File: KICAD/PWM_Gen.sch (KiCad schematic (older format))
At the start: 0 parts

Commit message: labels dans les blocks
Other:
- note added: "Astuce: utilisez le ~~ devant un label pour créer des signaux ~barre"
- note added: "Entrées"
- note added: "Sorties"
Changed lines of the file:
@@
 Comment4 ""
 $EndDescr
+Text HLabel 5150 3050 0    50   Input ~ 0
+Ramp
+Text HLabel 5150 3150 0    50   Input ~ 0
+Feedback
+Text HLabel 5450 3050 2    50   Output ~ 0
+PWM
+Text HLabel 5450 3150 2    50   Output ~ 0
+~PWM
+Text Notes 4850 3300 0    50   ~ 0
+Entrées
+Text Notes 4050 3600 0    50   ~ 0
+Astuce: utilisez le ~~ devant un label pour créer des signaux ~barre
+Text Notes 5450 3300 0    50   ~ 0
+Sorties
+Wire Notes Line
+	5400 2950 5800 2950
+Wire Notes Line
+	5800 2950 5800 3350
+Wire Notes Line
+	5800 3350 5400 3350
+Wire Notes Line
+	5400 2950 5400 3350
+Wire Notes Line
+	5250 2950 5250 3350
+Wire Notes Line
+	5250 3350 4700 3350
+Wire Notes Line
+	4700 3350 4700 2950
+Wire Notes Line
+	4700 2950 5250 2950
 $EndSCHEMATC

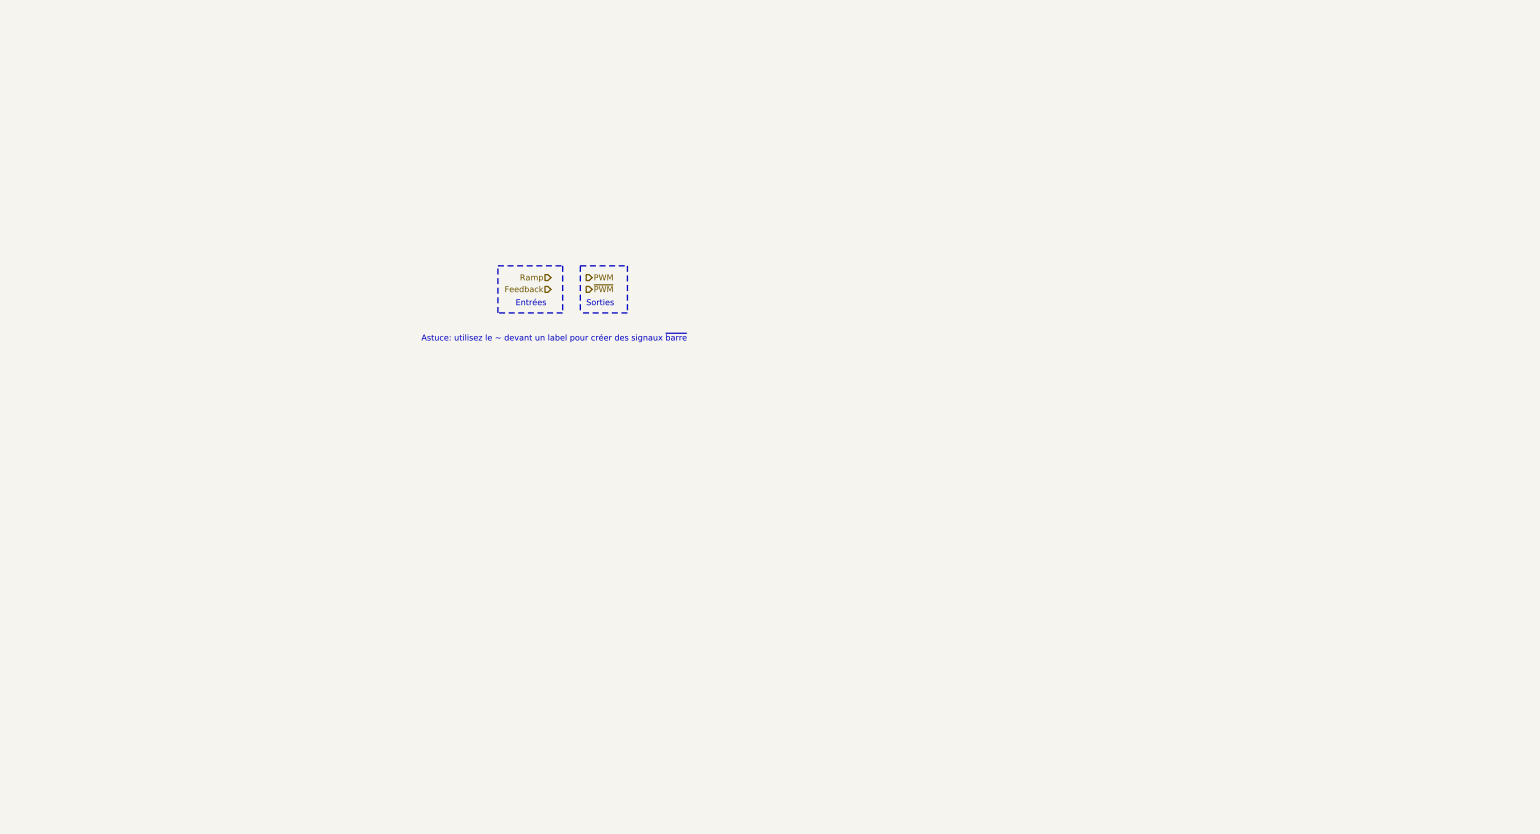
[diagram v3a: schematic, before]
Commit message: added draft pwm gen & pid
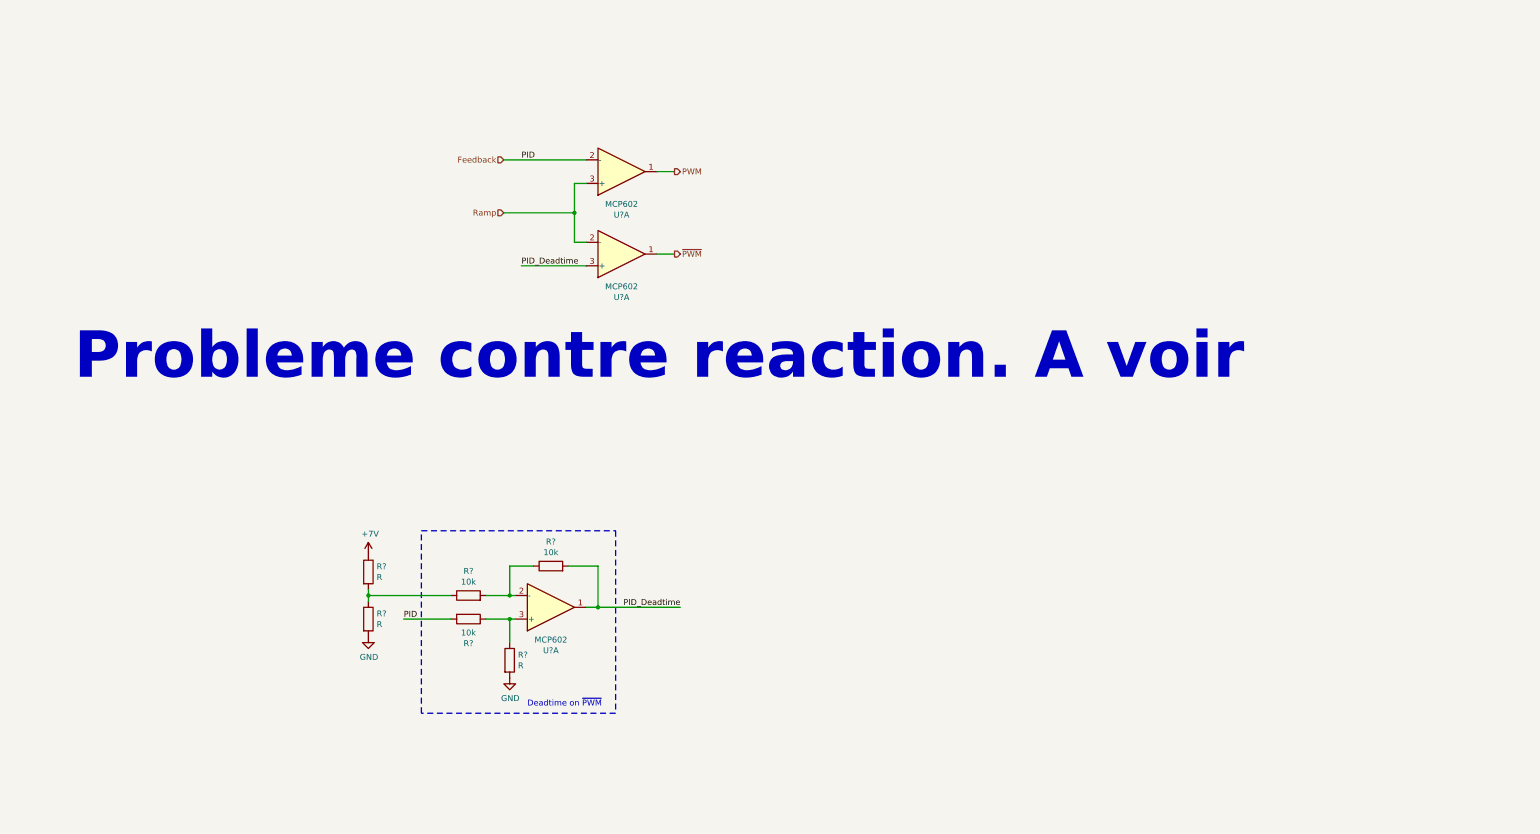
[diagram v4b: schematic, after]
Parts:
- added R? (x3): 10k, symbol Device:R
- added R? (x3): R, symbol Device:R
- added U? (x3): MCP602, symbol Amplifier_Operational:MCP602
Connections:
- net Feedback: now also R?.2, U?.2 (-)
- net PWM: now also U?.1
- net Ramp: now also U?.2 (-), U?.3 (+)
- net ~PWM: now also U?.1
- new net: R?.1, R?.2, U?.2 (-)
- new net: R?.1, R?.1, U?.3 (+)
- new net: R?.1, R?.1, R?.2
- new net +7V: R?.1
- new net GND: R?.2, R?.2
- new net PID_Deadtime: R?.2, U?.1, U?.3 (+)
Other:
- note added: "Deadtime on ~PWM"
- note added: "Probleme contre reaction. A voir\n"
- note removed: "Astuce: utilisez le ~~ devant un label pour créer des signaux ~barre"
- note removed: "Entrées"
- note removed: "Sorties"

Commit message: a ton of new stuff. V0.8
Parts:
- added C?: 100n, symbol Device:C
- added U?: MCP602, symbol Amplifier_Operational:MCP602
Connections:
- net Feedback: now also U?.3 (+); no longer U?.2 (-)
- net GND: now also C?.2, U?.8 (V+)
- net PID_Deadtime: no longer U?.3 (+)
- net Ramp: now also U?.2 (-), U?.3 (+); no longer U?.2 (-), U?.3 (+)
- net VDeadTime: now reaches R?.1, R?.1, R?.2
- net +7V renamed VREF
- new net Feedback_Deadtime: U?.2 (-)
- new net VCC: C?.1, U?.4 (V-)
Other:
- note added: "Tension deadtime"
- moved on the sheet: R?, U?A

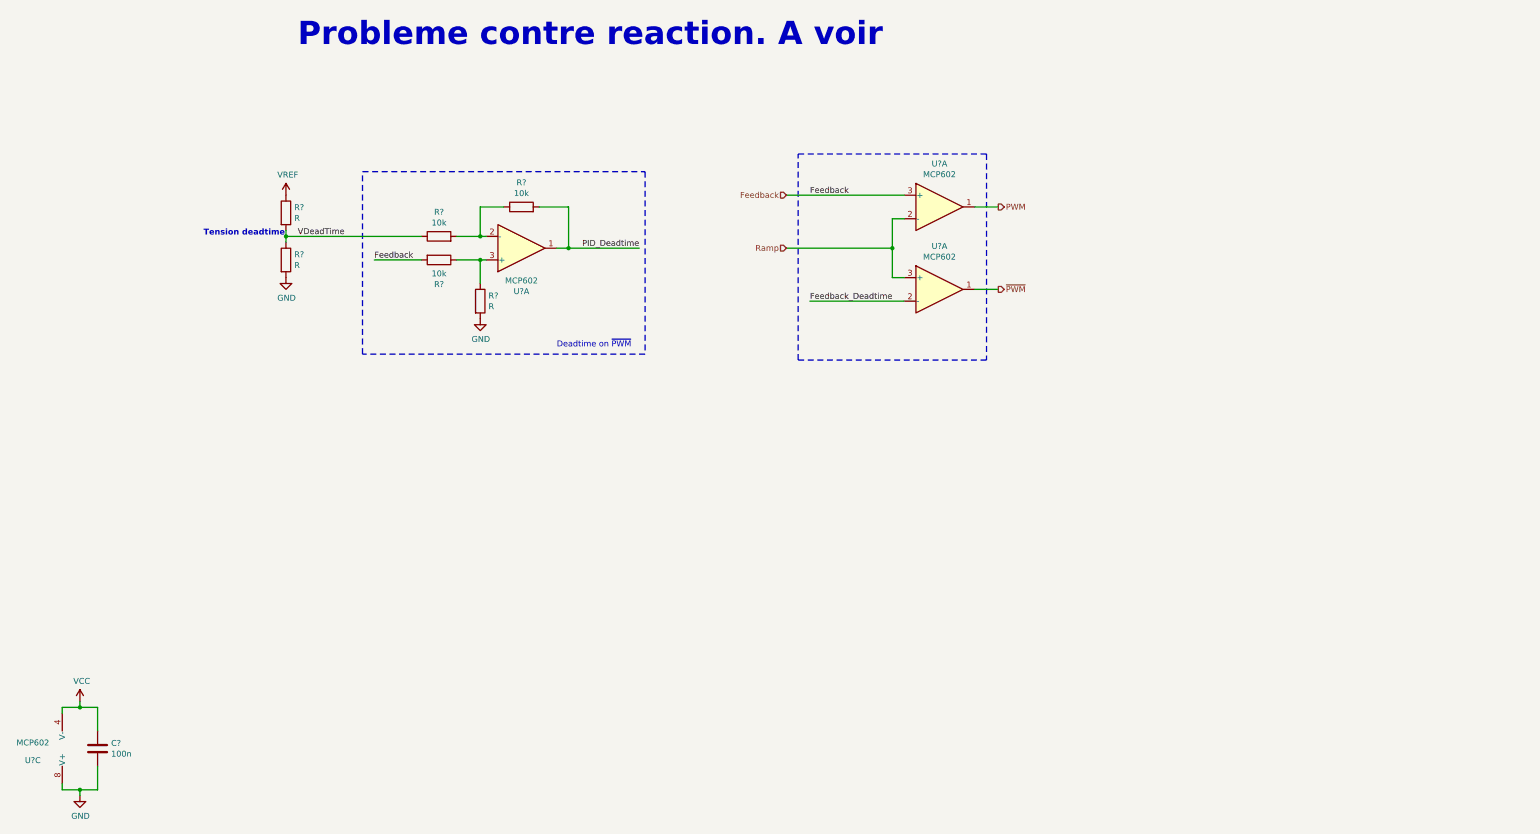
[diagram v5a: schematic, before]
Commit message: PID + PWM + RAMP finished
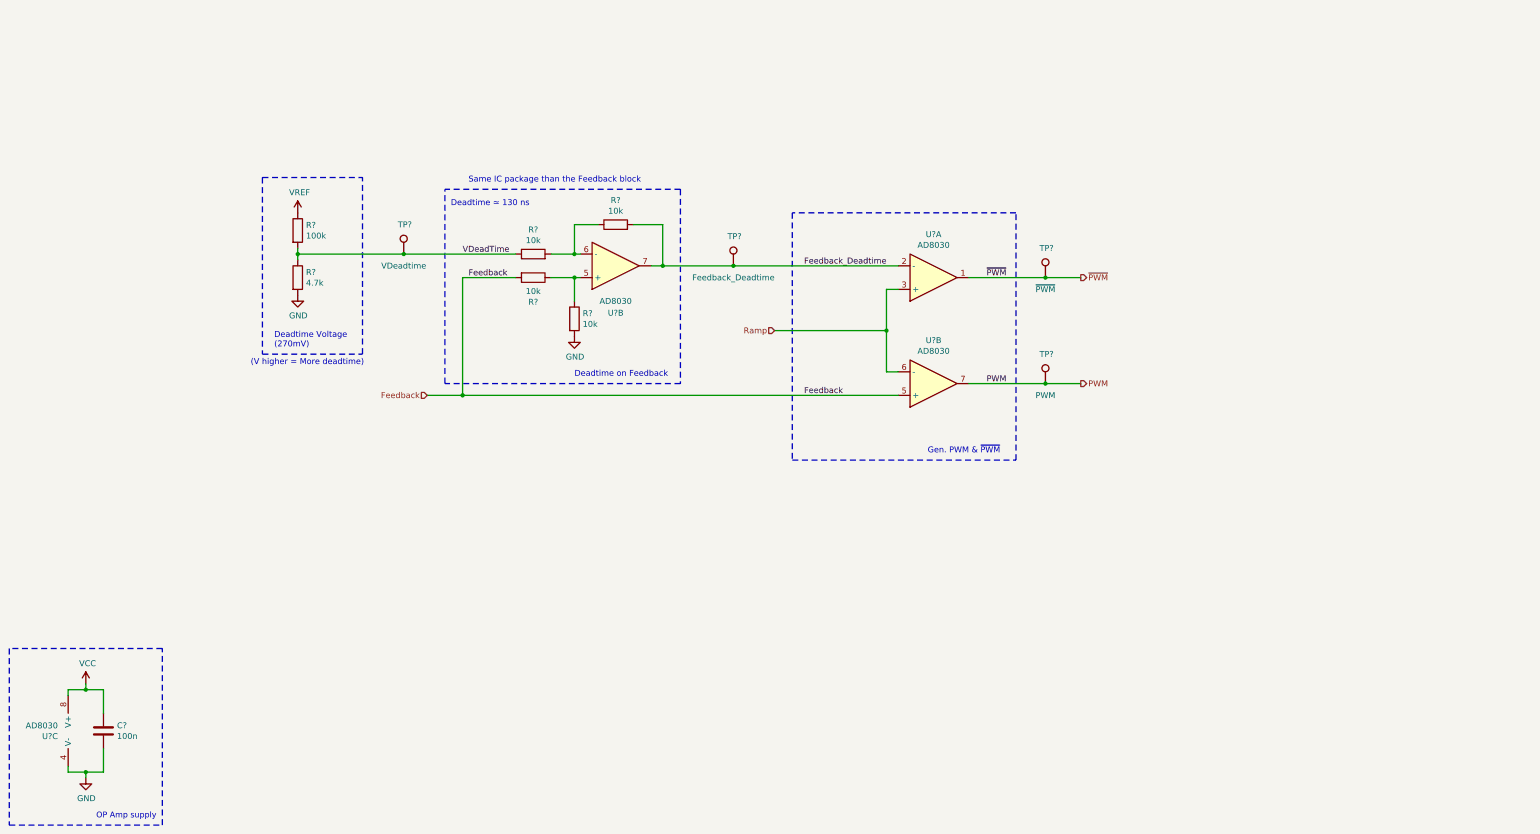
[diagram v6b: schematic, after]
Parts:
- removed C?: 100n, symbol Device:C
- removed U? (x4): MCP602, symbol Amplifier_Operational:MCP602
- added C?: 100n, Capacitor_SMD:C_0805_2012Metric_Pad1.15x1.40mm_HandSolder, symbol Device:C
- added TP?: VDeadtime, symbol Connector:TestPoint
- added TP?: Feedback_Deadtime, symbol Connector:TestPoint
- added TP?: ~PWM, symbol Connector:TestPoint
- added TP?: PWM, symbol Connector:TestPoint
- added U? (x4): AD8030, symbol Sesame:AD8030
- R? (x3): footprint (none) -> Resistor_SMD:R_0805_2012Metric_Pad1.15x1.40mm_HandSolder
- R?: value R -> 10k; footprint (none) -> Resistor_SMD:R_0805_2012Metric_Pad1.15x1.40mm_HandSolder
- R?: value R -> 100k; footprint (none) -> Resistor_SMD:R_0805_2012Metric_Pad1.15x1.40mm_HandSolder
- R?: value R -> 4.7k; footprint (none) -> Resistor_SMD:R_0805_2012Metric_Pad1.15x1.40mm_HandSolder
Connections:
- net PID_Deadtime is gone; now on net Feedback_Deadtime: R?.2
- net Feedback: now also U?.5 (+)
- net Feedback_Deadtime: now also TP?.1, U?.2 (-), U?.7
- net GND: now also C?.2, U?.4 (V-)
- net PWM: now also TP?.1, U?.7
- net Ramp: now also U?.3 (+), U?.6 (-)
- net VCC: now also C?.1, U?.8 (V+)
- net VDeadTime: now also TP?.1
- net ~PWM: now also TP?.1, U?.1
- net at R?.1, R?.2: now also U?.6 (-)
- net at R?.1, R?.1: now also U?.5 (+)
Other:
- note added: "(V higher = More deadtime)"
- note added: "Deadtime Voltage\n(270mV)"
- note added: "Deadtime on Feedback"
- note added: "Deadtime ≃ 130 ns"
- note added: "Gen. PWM & ~PWM"
- note added: "OP Amp supply"
- note added: "Same IC package than the Feedback block"
- note removed: "Deadtime on ~PWM"
- note removed: "Probleme contre reaction. A voir\n"
- note removed: "Tension deadtime"
- moved on the sheet: R?

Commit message: mainly footprints
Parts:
- U1, U2: renamed from U?; footprint (none) -> Package_SO:SO-8_3.9x4.9mm_P1.27mm
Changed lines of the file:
@@
 $Descr A4 11693 8268
 encoding utf-8
-Sheet 3 16
+Sheet 2 16
 Title "SESAME"
 Date ""
@@
 Same IC package than the Feedback block
 $Comp
-L Sesame:AD8030 U?
+L Sesame:AD8030 U2
 U 1 1 6128401D
 P 8400 3050
-F 0 "U?" H 8400 2683 50  0000 C CNN
+F 0 "U2" H 8400 2683 50  0000 C CNN
 F 1 "AD8030" H 8400 2774 50  0000 C CNN
-F 2 "" H 8400 3050 50  0001 C CNN
+F 2 "Package_SO:SO-8_3.9x4.9mm_P1.27mm" H 8400 3050 50  0001 C CNN
 F 3 "~" H 8400 3050 50  0001 C CNN
 	1    8400 3050
@@
 $EndComp
 $Comp
-L Sesame:AD8030 U?
+L Sesame:AD8030 U2
 U 2 1 61284FE7
 P 8400 3950
-F 0 "U?" H 8400 3583 50  0000 C CNN
+F 0 "U2" H 8400 3583 50  0000 C CNN
 F 1 "AD8030" H 8400 3674 50  0000 C CNN
-F 2 "" H 8400 3950 50  0001 C CNN
+F 2 "Package_SO:SO-8_3.9x4.9mm_P1.27mm" H 8400 3950 50  0001 C CNN
 F 3 "~" H 8400 3950 50  0001 C CNN
 	2    8400 3950
@@
 $EndComp
 $Comp
-L Sesame:AD8030 U?
+L Sesame:AD8030 U1
 U 2 1 6128D784
 P 5700 2950
-F 0 "U?" H 5700 3350 50  0000 C CNN
+F 0 "U1" H 5700 3350 50  0000 C CNN
 F 1 "AD8030" H 5700 3250 50  0000 C CNN
-F 2 "" H 5700 2950 50  0001 C CNN
+F 2 "Package_SO:SO-8_3.9x4.9mm_P1.27mm" H 5700 2950 50  0001 C CNN
 F 3 "~" H 5700 2950 50  0001 C CNN
 	2    5700 2950
@@
 $EndComp
 $Comp
-L Sesame:AD8030 U?
+L Sesame:AD8030 U2
 U 3 1 612CB373
 P 1150 6900
-AR Path="/60F1AF26/612CB373" Ref="U?"  Part="3"
+AR Path="/60F1AF26/612CB373" Ref="U2"  Part="3"
 AR Path="/60F1B237/612CB373" Ref="U?"  Part="3"
-F 0 "U?" H 963 6854 50  0000 R CNN
+F 0 "U2" H 963 6854 50  0000 R CNN
 F 1 "AD8030" H 963 6945 50  0000 R CNN
-F 2 "" H 1150 6900 50  0001 C CNN
+F 2 "Package_SO:SO-8_3.9x4.9mm_P1.27mm" H 1150 6900 50  0001 C CNN
 F 3 "~" H 1150 6900 50  0001 C CNN
 	3    1150 6900

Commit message: revex with jmt
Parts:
- R? (x4): value 10k -> 100k
- TP?: value VDeadtime -> TP_NOP
- TP?: value Feedback_Deadtime -> TP_POP
- TP?: value ~PWM -> TP_POP
- TP?: value PWM -> TP_POP
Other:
- moved on the sheet: TP?, U2A, U2B
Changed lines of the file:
@@
 $Descr A4 11693 8268
 encoding utf-8
-Sheet 2 16
+Sheet 16 16
 Title "SESAME"
 Date ""
@@
 AR Path="/60F1AF26/613D641B" Ref="R?"  Part="1"
 F 0 "R?" V 5207 3050 50  0000 C CNN
-F 1 "10k" V 5116 3050 50  0000 C CNN
+F 1 "100k" V 5116 3050 50  0000 C CNN
 F 2 "Resistor_SMD:R_0805_2012Metric_Pad1.15x1.40mm_HandSolder" V 4930 3050 50  0001 C CNN
 F 3 "~" H 5000 3050 50  0001 C CNN
@@
 AR Path="/60F1AF26/613D6415" Ref="R?"  Part="1"
 F 0 "R?" V 5207 2850 50  0000 C CNN
-F 1 "10k" V 5116 2850 50  0000 C CNN
+F 1 "100k" V 5116 2850 50  0000 C CNN
 F 2 "Resistor_SMD:R_0805_2012Metric_Pad1.15x1.40mm_HandSolder" V 4930 2850 50  0001 C CNN
 F 3 "~" H 5000 2850 50  0001 C CNN
@@
 AR Path="/60F1AF26/613D6429" Ref="R?"  Part="1"
 F 0 "R?" H 5420 3446 50  0000 L CNN
-F 1 "10k" H 5420 3355 50  0000 L CNN
+F 1 "100k" H 5420 3355 50  0000 L CNN
 F 2 "Resistor_SMD:R_0805_2012Metric_Pad1.15x1.40mm_HandSolder" V 5280 3400 50  0001 C CNN
 F 3 "~" H 5350 3400 50  0001 C CNN
@@
 Connection ~ 6100 2950
 Wire Wire Line
-	8000 3150 8000 3500
-Wire Wire Line
-	8000 3500 8000 3850
-Connection ~ 8000 3500
-Text Notes 8350 4550 0    50   ~ 0
+	7800 3150 7800 3500
+Wire Wire Line
+	7800 3500 7800 3850
+Connection ~ 7800 3500
+Text Notes 8150 4550 0    50   ~ 0
 Gen. PWM & ~PWM
 Wire Wire Line
-	9650 3950 9350 3950
-Wire Notes Line
-	7200 4600 9100 4600
-Wire Notes Line
-	9100 4600 9100 2500
-Wire Wire Line
-	7050 3500 8000 3500
-Text Label 7300 4050 0    50   ~ 0
+	9450 3950 9150 3950
+Wire Notes Line
+	7000 4600 8900 4600
+Wire Notes Line
+	8900 4600 8900 2500
+Wire Wire Line
+	6850 3500 7800 3500
+Text Label 7100 4050 0    50   ~ 0
 Feedback
-Text Label 7300 2950 0    50   ~ 0
+Text Label 7100 2950 0    50   ~ 0
 Feedback_Deadtime
 Wire Wire Line
-	8000 3850 8100 3850
-Wire Wire Line
-	8100 3150 8000 3150
-Wire Wire Line
-	8700 3050 9350 3050
-Text HLabel 9650 3050 2    50   Output ~ 0
+	7800 3850 7900 3850
+Wire Wire Line
+	7900 3150 7800 3150
+Wire Wire Line
+	8500 3050 9150 3050
+Text HLabel 9450 3050 2    50   Output ~ 0
 ~PWM
-Text HLabel 9650 3950 2    50   Output ~ 0
+Text HLabel 9450 3950 2    50   Output ~ 0
 PWM
-Text HLabel 7050 3500 0    50   Input ~ 0
+Text HLabel 6850 3500 0    50   Input ~ 0
 Ramp
 Wire Notes Line
-	9100 2500 7200 2500
-Wire Notes Line
-	7200 2500 7200 4600
+	8900 2500 7000 2500
+Wire Notes Line
+	7000 2500 7000 4600
 Wire Wire Line
 	4100 4050 4400 4050
 Wire Wire Line
-	4400 4050 8100 4050
+	4400 4050 7900 4050
 Text Notes 4450 2250 0    50   ~ 0
 Same IC package than the Feedback block
@@
 L Sesame:AD8030 U2
 U 1 1 6128401D
-P 8400 3050
-F 0 "U2" H 8400 2683 50  0000 C CNN
-F 1 "AD8030" H 8400 2774 50  0000 C CNN
-F 2 "Package_SO:SO-8_3.9x4.9mm_P1.27mm" H 8400 3050 50  0001 C CNN
-F 3 "~" H 8400 3050 50  0001 C CNN
-	1    8400 3050
+P 8200 3050
+F 0 "U2" H 8200 2683 50  0000 C CNN
+F 1 "AD8030" H 8200 2774 50  0000 C CNN
+F 2 "Package_SO:SO-8_3.9x4.9mm_P1.27mm" H 8200 3050 50  0001 C CNN
+F 3 "~" H 8200 3050 50  0001 C CNN
+	1    8200 3050
 	1    0    0    1
 $EndComp
@@
 L Sesame:AD8030 U2
 U 2 1 61284FE7
-P 8400 3950
-F 0 "U2" H 8400 3583 50  0000 C CNN
-F 1 "AD8030" H 8400 3674 50  0000 C CNN
-F 2 "Package_SO:SO-8_3.9x4.9mm_P1.27mm" H 8400 3950 50  0001 C CNN
-F 3 "~" H 8400 3950 50  0001 C CNN
-	2    8400 3950
+P 8200 3950
+F 0 "U2" H 8200 3583 50  0000 C CNN
+F 1 "AD8030" H 8200 3674 50  0000 C CNN
+F 2 "Package_SO:SO-8_3.9x4.9mm_P1.27mm" H 8200 3950 50  0001 C CNN
+F 3 "~" H 8200 3950 50  0001 C CNN
+	2    8200 3950
 	1    0    0    1
 $EndComp
@@
 P 3900 2850
 F 0 "TP?" H 3850 3100 50  0000 L CNN
-F 1 "VDeadtime" H 3900 2750 50  0000 C CNN
+F 1 "TP_NOP" H 3900 2750 50  0000 C CNN
 F 2 "" H 4100 2850 50  0001 C CNN
 F 3 "~" H 4100 2850 50  0001 C CNN
@@
 L Connector:TestPoint TP?
 U 1 1 61299A59
-P 6700 2950
-F 0 "TP?" H 6650 3200 50  0000 L CNN
-F 1 "Feedback_Deadtime" H 6700 2850 50  0000 C CNN
-F 2 "" H 6900 2950 50  0001 C CNN
-F 3 "~" H 6900 2950 50  0001 C CNN
-	1    6700 2950
-	1    0    0    -1
-$EndComp
-Wire Wire Line
-	6100 2950 6700 2950
-Connection ~ 6700 2950
-Wire Wire Line
-	6700 2950 8100 2950
+P 6600 2950
+F 0 "TP?" H 6550 3200 50  0000 L CNN
+F 1 "TP_POP" H 6600 2850 50  0000 C CNN
+F 2 "" H 6800 2950 50  0001 C CNN
+F 3 "~" H 6800 2950 50  0001 C CNN
+	1    6600 2950
+	1    0    0    -1
+$EndComp
+Wire Wire Line
+	6100 2950 6600 2950
+Connection ~ 6600 2950
+Wire Wire Line
+	6600 2950 7900 2950
 $Comp
 L Connector:TestPoint TP?
 U 1 1 612A9FCA
-P 9350 3950
-F 0 "TP?" H 9300 4200 50  0000 L CNN
-F 1 "PWM" H 9350 3850 50  0000 C CNN
-F 2 "" H 9550 3950 50  0001 C CNN
-F 3 "~" H 9550 3950 50  0001 C CNN
-	1    9350 3950
-	1    0    0    -1
-$EndComp
-Connection ~ 9350 3050
-Wire Wire Line
-	9350 3050 9650 3050
-Connection ~ 9350 3950
-Wire Wire Line
-	9350 3950 8700 3950
+P 9150 3950
+F 0 "TP?" H 9100 4200 50  0000 L CNN
+F 1 "TP_POP" H 9150 3850 50  0000 C CNN
+F 2 "" H 9350 3950 50  0001 C CNN
+F 3 "~" H 9350 3950 50  0001 C CNN
+	1    9150 3950
+	1    0    0    -1
+$EndComp
+Connection ~ 9150 3050
+Wire Wire Line
+	9150 3050 9450 3050
+Connection ~ 9150 3950
+Wire Wire Line
+	9150 3950 8500 3950
 $Comp
 L Connector:TestPoint TP?
 U 1 1 612A923F
-P 9350 3050
-F 0 "TP?" H 9300 3300 50  0000 L CNN
-F 1 "~PWM" H 9350 2950 50  0000 C CNN
-F 2 "" H 9550 3050 50  0001 C CNN
-F 3 "~" H 9550 3050 50  0001 C CNN
-	1    9350 3050
+P 9150 3050
+F 0 "TP?" H 9100 3300 50  0000 L CNN
+F 1 "TP_POP" H 9150 2950 50  0000 C CNN
+F 2 "" H 9350 3050 50  0001 C CNN
+F 3 "~" H 9350 3050 50  0001 C CNN
+	1    9150 3050
 	1    0    0    -1
 $EndComp
@@
 	1    0    0    -1
 $EndComp
-Text Label 8850 3050 0    50   ~ 0
+Text Label 8650 3050 0    50   ~ 0
 ~PWM
-Text Label 8850 3950 0    50   ~ 0
+Text Label 8650 3950 0    50   ~ 0
 PWM
 Text Notes 4300 2450 0    50   ~ 0
@@
 AR Path="/60F1AF26/613D640F" Ref="R?"  Part="1"
 F 0 "R?" V 5907 2600 50  0000 C CNN
-F 1 "10k" V 5816 2600 50  0000 C CNN
+F 1 "100k" V 5816 2600 50  0000 C CNN
 F 2 "Resistor_SMD:R_0805_2012Metric_Pad1.15x1.40mm_HandSolder" V 5630 2600 50  0001 C CNN
 F 3 "~" H 5700 2600 50  0001 C CNN
